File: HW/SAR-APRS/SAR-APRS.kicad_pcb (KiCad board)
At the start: 2 copper layers, 1 part

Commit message: update
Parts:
- removed A1: Arduino_Nano_v3.x, Modules:Arduino_Nano
- added U1: DRA818V, APRS_modules:DRA818, F.Cu at (190.2, 96.0)
- added U2: arduino_mini_clone, APRS_modules:arduino_mini_clone, F.Cu at (152.0, 96.0)

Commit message: update
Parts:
- added U3: ATMEGA328P-MMH, Housings_DFN_QFN:QFN-28-1EP_4x4mm_Pitch0.4mm, F.Cu at (162.1, 112.9)
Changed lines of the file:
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@@
     (tracks 0)
     (zones 0)
-    (modules 2)
-    (nets 57)
+    (modules 3)
+    (nets 85)
   )
   (page A4)
@@
   (net 55 "Net-(U1-Pad6)")
   (net 56 "Net-(U1-Pad7)")
+  (net 57 "Net-(U3-Pad1)")
+  (net 58 "Net-(U3-Pad2)")
+  (net 59 "Net-(U3-Pad3)")
+  (net 60 "Net-(U3-Pad4)")
+  (net 61 "Net-(U3-Pad5)")
+  (net 62 "Net-(U3-Pad6)")
+  (net 63 "Net-(U3-Pad7)")
+  (net 64 "Net-(U3-Pad8)")
+  (net 65 "Net-(U3-Pad9)")
+  (net 66 "Net-(U3-Pad10)")
+  (net 67 "Net-(U3-Pad11)")
+  (net 68 "Net-(U3-Pad12)")
+  (net 69 "Net-(U3-Pad13)")
+  (net 70 "Net-(U3-Pad14)")
+  (net 71 "Net-(U3-Pad15)")
+  (net 72 "Net-(U3-Pad16)")
+  (net 73 "Net-(U3-Pad17)")
+  (net 74 "Net-(U3-Pad18)")
+  (net 75 "Net-(U3-Pad19)")
+  (net 76 "Net-(U3-Pad20)")
+  (net 77 "Net-(U3-Pad21)")
+  (net 78 "Net-(U3-Pad22)")
+  (net 79 "Net-(U3-Pad23)")
+  (net 80 "Net-(U3-Pad24)")
+  (net 81 "Net-(U3-Pad25)")
+  (net 82 "Net-(U3-Pad26)")
+  (net 83 "Net-(U3-Pad27)")
+  (net 84 "Net-(U3-Pad28)")
   (net_class Default "This is the default net class."
     (clearance 0.2)
@@
     (add_net "Net-(U2-Pad8)")
     (add_net "Net-(U2-Pad9)")
+    (add_net "Net-(U3-Pad1)")
+    (add_net "Net-(U3-Pad10)")
+    (add_net "Net-(U3-Pad11)")
+    (add_net "Net-(U3-Pad12)")
+    (add_net "Net-(U3-Pad13)")
+    (add_net "Net-(U3-Pad14)")
+    (add_net "Net-(U3-Pad15)")
+    (add_net "Net-(U3-Pad16)")
+    (add_net "Net-(U3-Pad17)")
+    (add_net "Net-(U3-Pad18)")
+    (add_net "Net-(U3-Pad19)")
+    (add_net "Net-(U3-Pad2)")
+    (add_net "Net-(U3-Pad20)")
+    (add_net "Net-(U3-Pad21)")
+    (add_net "Net-(U3-Pad22)")
+    (add_net "Net-(U3-Pad23)")
+    (add_net "Net-(U3-Pad24)")
+    (add_net "Net-(U3-Pad25)")
+    (add_net "Net-(U3-Pad26)")
+    (add_net "Net-(U3-Pad27)")
+    (add_net "Net-(U3-Pad28)")
+    (add_net "Net-(U3-Pad3)")
+    (add_net "Net-(U3-Pad4)")
+    (add_net "Net-(U3-Pad5)")
+    (add_net "Net-(U3-Pad6)")
+    (add_net "Net-(U3-Pad7)")
+    (add_net "Net-(U3-Pad8)")
+    (add_net "Net-(U3-Pad9)")
+  )
+  (module Housings_DFN_QFN:QFN-28-1EP_4x4mm_Pitch0.4mm (layer F.Cu)
+    (at 162.1 112.9)
+    (descr "28-Lead Plastic Quad Flat, No Lead Package (MK) - 4x4x0.9 mm Body [QFN]; (see Microchip Packaging Specification 00000049BS.pdf)")
+    (tags "QFN 0.4")
+    (attr smd)
+    (fp_text reference U3 (at 0 -3.35) (layer F.SilkS)
+      (effects (font (size 1 1) (thickness 0.15)))
+    )
+    (fp_text value ATMEGA328P-MMH (at 0 3.35) (layer F.Fab)
+      (effects (font (size 1 1) (thickness 0.15)))
+    )
+    (fp_line (start -1 -2) (end 2 -2) (layer F.Fab) (width 0.15))
+    (fp_line (start 2 -2) (end 2 2) (layer F.Fab) (width 0.15))
+    (fp_line (start 2 2) (end -2 2) (layer F.Fab) (width 0.15))
+    (fp_line (start -2 2) (end -2 -1) (layer F.Fab) (width 0.15))
+    (fp_line (start -2 -1) (end -1 -2) (layer F.Fab) (width 0.15))
+    (fp_line (start -2.6 -2.6) (end -2.6 2.6) (layer F.CrtYd) (width 0.05))
+    (fp_line (start 2.6 -2.6) (end 2.6 2.6) (layer F.CrtYd) (width 0.05))
+    (fp_line (start -2.6 -2.6) (end 2.6 -2.6) (layer F.CrtYd) (width 0.05))
+    (fp_line (start -2.6 2.6) (end 2.6 2.6) (layer F.CrtYd) (width 0.05))
+    (fp_line (start 2.15 -2.15) (end 2.15 -1.525) (layer F.SilkS) (width 0.15))
+    (fp_line (start -2.15 2.15) (end -2.15 1.525) (layer F.SilkS) (width 0.15))
+    (fp_line (start 2.15 2.15) (end 2.15 1.525) (layer F.SilkS) (width 0.15))
+    (fp_line (start -2.15 -2.15) (end -1.525 -2.15) (layer F.SilkS) (width 0.15))
+    (fp_line (start -2.15 2.15) (end -1.525 2.15) (layer F.SilkS) (width 0.15))
+    (fp_line (start 2.15 2.15) (end 1.525 2.15) (layer F.SilkS) (width 0.15))
+    (fp_line (start 2.15 -2.15) (end 1.525 -2.15) (layer F.SilkS) (width 0.15))
+    (pad 1 smd rect (at -1.95 -1.2) (size 0.8 0.2) (layers F.Cu F.Paste F.Mask)
+      (net 57 "Net-(U3-Pad1)"))
+    (pad 2 smd rect (at -1.95 -0.8) (size 0.8 0.2) (layers F.Cu F.Paste F.Mask)
+      (net 58 "Net-(U3-Pad2)"))
+    (pad 3 smd rect (at -1.95 -0.4) (size 0.8 0.2) (layers F.Cu F.Paste F.Mask)
+      (net 59 "Net-(U3-Pad3)"))
+    (pad 4 smd rect (at -1.95 0) (size 0.8 0.2) (layers F.Cu F.Paste F.Mask)
+      (net 60 "Net-(U3-Pad4)"))
+    (pad 5 smd rect (at -1.95 0.4) (size 0.8 0.2) (layers F.Cu F.Paste F.Mask)
+      (net 61 "Net-(U3-Pad5)"))
+    (pad 6 smd rect (at -1.95 0.8) (size 0.8 0.2) (layers F.Cu F.Paste F.Mask)
+      (net 62 "Net-(U3-Pad6)"))
+    (pad 7 smd rect (at -1.95 1.2) (size 0.8 0.2) (layers F.Cu F.Paste F.Mask)
+      (net 63 "Net-(U3-Pad7)"))
+    (pad 8 smd rect (at -1.2 1.95 90) (size 0.8 0.2) (layers F.Cu F.Paste F.Mask)
+      (net 64 "Net-(U3-Pad8)"))
+    (pad 9 smd rect (at -0.8 1.95 90) (size 0.8 0.2) (layers F.Cu F.Paste F.Mask)
+      (net 65 "Net-(U3-Pad9)"))
+    (pad 10 smd rect (at -0.4 1.95 90) (size 0.8 0.2) (layers F.Cu F.Paste F.Mask)
+      (net 66 "Net-(U3-Pad10)"))
+    (pad 11 smd rect (at 0 1.95 90) (size 0.8 0.2) (layers F.Cu F.Paste F.Mask)
+      (net 67 "Net-(U3-Pad11)"))
+    (pad 12 smd rect (at 0.4 1.95 90) (size 0.8 0.2) (layers F.Cu F.Paste F.Mask)
+      (net 68 "Net-(U3-Pad12)"))
+    (pad 13 smd rect (at 0.8 1.95 90) (size 0.8 0.2) (layers F.Cu F.Paste F.Mask)
+      (net 69 "Net-(U3-Pad13)"))
+    (pad 14 smd rect (at 1.2 1.95 90) (size 0.8 0.2) (layers F.Cu F.Paste F.Mask)
+      (net 70 "Net-(U3-Pad14)"))
+    (pad 15 smd rect (at 1.95 1.2) (size 0.8 0.2) (layers F.Cu F.Paste F.Mask)
+      (net 71 "Net-(U3-Pad15)"))
+    (pad 16 smd rect (at 1.95 0.8) (size 0.8 0.2) (layers F.Cu F.Paste F.Mask)
+      (net 72 "Net-(U3-Pad16)"))
+    (pad 17 smd rect (at 1.95 0.4) (size 0.8 0.2) (layers F.Cu F.Paste F.Mask)
+      (net 73 "Net-(U3-Pad17)"))
+    (pad 18 smd rect (at 1.95 0) (size 0.8 0.2) (layers F.Cu F.Paste F.Mask)
+      (net 74 "Net-(U3-Pad18)"))
+    (pad 19 smd rect (at 1.95 -0.4) (size 0.8 0.2) (layers F.Cu F.Paste F.Mask)
+      (net 75 "Net-(U3-Pad19)"))
+    (pad 20 smd rect (at 1.95 -0.8) (size 0.8 0.2) (layers F.Cu F.Paste F.Mask)
+      (net 76 "Net-(U3-Pad20)"))
+    (pad 21 smd rect (at 1.95 -1.2) (size 0.8 0.2) (layers F.Cu F.Paste F.Mask)
+      (net 77 "Net-(U3-Pad21)"))
+    (pad 22 smd rect (at 1.2 -1.95 90) (size 0.8 0.2) (layers F.Cu F.Paste F.Mask)
+      (net 78 "Net-(U3-Pad22)"))
+    (pad 23 smd rect (at 0.8 -1.95 90) (size 0.8 0.2) (layers F.Cu F.Paste F.Mask)
+      (net 79 "Net-(U3-Pad23)"))
+    (pad 24 smd rect (at 0.4 -1.95 90) (size 0.8 0.2) (layers F.Cu F.Paste F.Mask)
+      (net 80 "Net-(U3-Pad24)"))
+    (pad 25 smd rect (at 0 -1.95 90) (size 0.8 0.2) (layers F.Cu F.Paste F.Mask)
+      (net 81 "Net-(U3-Pad25)"))
+    (pad 26 smd rect (at -0.4 -1.95 90) (size 0.8 0.2) (layers F.Cu F.Paste F.Mask)
+      (net 82 "Net-(U3-Pad26)"))
+    (pad 27 smd rect (at -0.8 -1.95 90) (size 0.8 0.2) (layers F.Cu F.Paste F.Mask)
+      (net 83 "Net-(U3-Pad27)"))
+    (pad 28 smd rect (at -1.2 -1.95 90) (size 0.8 0.2) (layers F.Cu F.Paste F.Mask)
+      (net 84 "Net-(U3-Pad28)"))
+    (pad 29 smd rect (at 0.6 0.6) (size 1.2 1.2) (layers F.Cu F.Paste F.Mask)
+      (solder_paste_margin_ratio -0.2))
+    (pad 29 smd rect (at 0.6 -0.6) (size 1.2 1.2) (layers F.Cu F.Paste F.Mask)
+      (solder_paste_margin_ratio -0.2))
+    (pad 29 smd rect (at -0.6 0.6) (size 1.2 1.2) (layers F.Cu F.Paste F.Mask)
+      (solder_paste_margin_ratio -0.2))
+    (pad 29 smd rect (at -0.6 -0.6) (size 1.2 1.2) (layers F.Cu F.Paste F.Mask)
+      (solder_paste_margin_ratio -0.2))
+    (model ${KISYS3DMOD}/Housings_DFN_QFN.3dshapes/QFN-28-1EP_4x4mm_Pitch0.4mm.wrl
+      (at (xyz 0 0 0))
+      (scale (xyz 1 1 1))
+      (rotate (xyz 0 0 0))
+    )
   )
   (module APRS_modules:DRA818 (layer F.Cu)

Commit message: update
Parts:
- removed U3: ATMEGA328P-MMH, Housings_DFN_QFN:QFN-28-1EP_4x4mm_Pitch0.4mm
- added J1: uFl, w_conn_rf:coaxial_u.fl-r-smt-1, F.Cu at (147.0, 78.0)
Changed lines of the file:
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@@
-(kicad_pcb (version 20171130) (host pcbnew "(6.0.0-rc1-dev-347-gd8782b751)")
+(kicad_pcb (version 20171130) (host pcbnew "(6.0.0-rc1-dev-909-gb389236a7)")
   (general
     (thickness 1.6)
@@
     (zones 0)
     (modules 3)
-    (nets 85)
+    (nets 59)
   )
   (page A4)
@@
     (pad_drill 0.762)
     (pad_to_mask_clearance 0.2)
+    (solder_mask_min_width 0.25)
     (aux_axis_origin 0 0)
     (visible_elements 7FFFFFFF)
@@
   (net 55 "Net-(U1-Pad6)")
   (net 56 "Net-(U1-Pad7)")
-  (net 57 "Net-(U3-Pad1)")
-  (net 58 "Net-(U3-Pad2)")
-  (net 59 "Net-(U3-Pad3)")
-  (net 60 "Net-(U3-Pad4)")
-  (net 61 "Net-(U3-Pad5)")
-  (net 62 "Net-(U3-Pad6)")
-  (net 63 "Net-(U3-Pad7)")
-  (net 64 "Net-(U3-Pad8)")
-  (net 65 "Net-(U3-Pad9)")
-  (net 66 "Net-(U3-Pad10)")
-  (net 67 "Net-(U3-Pad11)")
-  (net 68 "Net-(U3-Pad12)")
-  (net 69 "Net-(U3-Pad13)")
-  (net 70 "Net-(U3-Pad14)")
-  (net 71 "Net-(U3-Pad15)")
-  (net 72 "Net-(U3-Pad16)")
-  (net 73 "Net-(U3-Pad17)")
-  (net 74 "Net-(U3-Pad18)")
-  (net 75 "Net-(U3-Pad19)")
-  (net 76 "Net-(U3-Pad20)")
-  (net 77 "Net-(U3-Pad21)")
-  (net 78 "Net-(U3-Pad22)")
-  (net 79 "Net-(U3-Pad23)")
-  (net 80 "Net-(U3-Pad24)")
-  (net 81 "Net-(U3-Pad25)")
-  (net 82 "Net-(U3-Pad26)")
-  (net 83 "Net-(U3-Pad27)")
-  (net 84 "Net-(U3-Pad28)")
+  (net 57 "Net-(J1-Pad1)")
+  (net 58 GND)
   (net_class Default "This is the default net class."
     (clearance 0.2)
@@
     (uvia_dia 0.3)
     (uvia_drill 0.1)
+    (add_net GND)
+    (add_net "Net-(J1-Pad1)")
     (add_net "Net-(U1-Pad1)")
     (add_net "Net-(U1-Pad10)")
@@
     (add_net "Net-(U2-Pad8)")
     (add_net "Net-(U2-Pad9)")
-    (add_net "Net-(U3-Pad1)")
-    (add_net "Net-(U3-Pad10)")
-    (add_net "Net-(U3-Pad11)")
-    (add_net "Net-(U3-Pad12)")
-    (add_net "Net-(U3-Pad13)")
-    (add_net "Net-(U3-Pad14)")
-    (add_net "Net-(U3-Pad15)")
-    (add_net "Net-(U3-Pad16)")
-    (add_net "Net-(U3-Pad17)")
-    (add_net "Net-(U3-Pad18)")
-    (add_net "Net-(U3-Pad19)")
-    (add_net "Net-(U3-Pad2)")
-    (add_net "Net-(U3-Pad20)")
-    (add_net "Net-(U3-Pad21)")
-    (add_net "Net-(U3-Pad22)")
-    (add_net "Net-(U3-Pad23)")
-    (add_net "Net-(U3-Pad24)")
-    (add_net "Net-(U3-Pad25)")
-    (add_net "Net-(U3-Pad26)")
-    (add_net "Net-(U3-Pad27)")
-    (add_net "Net-(U3-Pad28)")
-    (add_net "Net-(U3-Pad3)")
-    (add_net "Net-(U3-Pad4)")
-    (add_net "Net-(U3-Pad5)")
-    (add_net "Net-(U3-Pad6)")
-    (add_net "Net-(U3-Pad7)")
-    (add_net "Net-(U3-Pad8)")
-    (add_net "Net-(U3-Pad9)")
-  )
-  (module Housings_DFN_QFN:QFN-28-1EP_4x4mm_Pitch0.4mm (layer F.Cu)
-    (at 162.1 112.9)
-    (descr "28-Lead Plastic Quad Flat, No Lead Package (MK) - 4x4x0.9 mm Body [QFN]; (see Microchip Packaging Specification 00000049BS.pdf)")
-    (tags "QFN 0.4")
-    (attr smd)
-    (fp_text reference U3 (at 0 -3.35) (layer F.SilkS)
-      (effects (font (size 1 1) (thickness 0.15)))
+  )
+  (module w_conn_rf:coaxial_u.fl-r-smt-1 (layer F.Cu)
+    (at 147 78)
+    (descr "Ultra small surface mount coaxial connector, Hirose U.FL-R-SMT-1")
+    (fp_text reference J1 (at 0 -2.1) (layer F.SilkS)
+      (effects (font (size 0.5 0.5) (thickness 0.1)))
     )
-    (fp_text value ATMEGA328P-MMH (at 0 3.35) (layer F.Fab)
-      (effects (font (size 1 1) (thickness 0.15)))
+    (fp_text value uFl (at 0 2.7) (layer F.SilkS)
+      (effects (font (size 0.5 0.5) (thickness 0.1)))
     )
-    (fp_line (start -1 -2) (end 2 -2) (layer F.Fab) (width 0.15))
-    (fp_line (start 2 -2) (end 2 2) (layer F.Fab) (width 0.15))
-    (fp_line (start 2 2) (end -2 2) (layer F.Fab) (width 0.15))
-    (fp_line (start -2 2) (end -2 -1) (layer F.Fab) (width 0.15))
-    (fp_line (start -2 -1) (end -1 -2) (layer F.Fab) (width 0.15))
-    (fp_line (start -2.6 -2.6) (end -2.6 2.6) (layer F.CrtYd) (width 0.05))
-    (fp_line (start 2.6 -2.6) (end 2.6 2.6) (layer F.CrtYd) (width 0.05))
-    (fp_line (start -2.6 -2.6) (end 2.6 -2.6) (layer F.CrtYd) (width 0.05))
-    (fp_line (start -2.6 2.6) (end 2.6 2.6) (layer F.CrtYd) (width 0.05))
-    (fp_line (start 2.15 -2.15) (end 2.15 -1.525) (layer F.SilkS) (width 0.15))
-    (fp_line (start -2.15 2.15) (end -2.15 1.525) (layer F.SilkS) (width 0.15))
-    (fp_line (start 2.15 2.15) (end 2.15 1.525) (layer F.SilkS) (width 0.15))
-    (fp_line (start -2.15 -2.15) (end -1.525 -2.15) (layer F.SilkS) (width 0.15))
-    (fp_line (start -2.15 2.15) (end -1.525 2.15) (layer F.SilkS) (width 0.15))
-    (fp_line (start 2.15 2.15) (end 1.525 2.15) (layer F.SilkS) (width 0.15))
-    (fp_line (start 2.15 -2.15) (end 1.525 -2.15) (layer F.SilkS) (width 0.15))
-    (pad 1 smd rect (at -1.95 -1.2) (size 0.8 0.2) (layers F.Cu F.Paste F.Mask)
-      (net 57 "Net-(U3-Pad1)"))
-    (pad 2 smd rect (at -1.95 -0.8) (size 0.8 0.2) (layers F.Cu F.Paste F.Mask)
-      (net 58 "Net-(U3-Pad2)"))
-    (pad 3 smd rect (at -1.95 -0.4) (size 0.8 0.2) (layers F.Cu F.Paste F.Mask)
-      (net 59 "Net-(U3-Pad3)"))
-    (pad 4 smd rect (at -1.95 0) (size 0.8 0.2) (layers F.Cu F.Paste F.Mask)
-      (net 60 "Net-(U3-Pad4)"))
-    (pad 5 smd rect (at -1.95 0.4) (size 0.8 0.2) (layers F.Cu F.Paste F.Mask)
-      (net 61 "Net-(U3-Pad5)"))
-    (pad 6 smd rect (at -1.95 0.8) (size 0.8 0.2) (layers F.Cu F.Paste F.Mask)
-      (net 62 "Net-(U3-Pad6)"))
-    (pad 7 smd rect (at -1.95 1.2) (size 0.8 0.2) (layers F.Cu F.Paste F.Mask)
-      (net 63 "Net-(U3-Pad7)"))
-    (pad 8 smd rect (at -1.2 1.95 90) (size 0.8 0.2) (layers F.Cu F.Paste F.Mask)
-      (net 64 "Net-(U3-Pad8)"))
-    (pad 9 smd rect (at -0.8 1.95 90) (size 0.8 0.2) (layers F.Cu F.Paste F.Mask)
-      (net 65 "Net-(U3-Pad9)"))
-    (pad 10 smd rect (at -0.4 1.95 90) (size 0.8 0.2) (layers F.Cu F.Paste F.Mask)
-      (net 66 "Net-(U3-Pad10)"))
-    (pad 11 smd rect (at 0 1.95 90) (size 0.8 0.2) (layers F.Cu F.Paste F.Mask)
-      (net 67 "Net-(U3-Pad11)"))
-    (pad 12 smd rect (at 0.4 1.95 90) (size 0.8 0.2) (layers F.Cu F.Paste F.Mask)
-      (net 68 "Net-(U3-Pad12)"))
-    (pad 13 smd rect (at 0.8 1.95 90) (size 0.8 0.2) (layers F.Cu F.Paste F.Mask)
-      (net 69 "Net-(U3-Pad13)"))
-    (pad 14 smd rect (at 1.2 1.95 90) (size 0.8 0.2) (layers F.Cu F.Paste F.Mask)
-      (net 70 "Net-(U3-Pad14)"))
-    (pad 15 smd rect (at 1.95 1.2) (size 0.8 0.2) (layers F.Cu F.Paste F.Mask)
-      (net 71 "Net-(U3-Pad15)"))
-    (pad 16 smd rect (at 1.95 0.8) (size 0.8 0.2) (layers F.Cu F.Paste F.Mask)
-      (net 72 "Net-(U3-Pad16)"))
-    (pad 17 smd rect (at 1.95 0.4) (size 0.8 0.2) (layers F.Cu F.Paste F.Mask)
-      (net 73 "Net-(U3-Pad17)"))
-    (pad 18 smd rect (at 1.95 0) (size 0.8 0.2) (layers F.Cu F.Paste F.Mask)
-      (net 74 "Net-(U3-Pad18)"))
-    (pad 19 smd rect (at 1.95 -0.4) (size 0.8 0.2) (layers F.Cu F.Paste F.Mask)
-      (net 75 "Net-(U3-Pad19)"))
-    (pad 20 smd rect (at 1.95 -0.8) (size 0.8 0.2) (layers F.Cu F.Paste F.Mask)
-      (net 76 "Net-(U3-Pad20)"))
-    (pad 21 smd rect (at 1.95 -1.2) (size 0.8 0.2) (layers F.Cu F.Paste F.Mask)
-      (net 77 "Net-(U3-Pad21)"))
-    (pad 22 smd rect (at 1.2 -1.95 90) (size 0.8 0.2) (layers F.Cu F.Paste F.Mask)
-      (net 78 "Net-(U3-Pad22)"))
-    (pad 23 smd rect (at 0.8 -1.95 90) (size 0.8 0.2) (layers F.Cu F.Paste F.Mask)
-      (net 79 "Net-(U3-Pad23)"))
-    (pad 24 smd rect (at 0.4 -1.95 90) (size 0.8 0.2) (layers F.Cu F.Paste F.Mask)
-      (net 80 "Net-(U3-Pad24)"))
-    (pad 25 smd rect (at 0 -1.95 90) (size 0.8 0.2) (layers F.Cu F.Paste F.Mask)
-      (net 81 "Net-(U3-Pad25)"))
-    (pad 26 smd rect (at -0.4 -1.95 90) (size 0.8 0.2) (layers F.Cu F.Paste F.Mask)
-      (net 82 "Net-(U3-Pad26)"))
-    (pad 27 smd rect (at -0.8 -1.95 90) (size 0.8 0.2) (layers F.Cu F.Paste F.Mask)
-      (net 83 "Net-(U3-Pad27)"))
-    (pad 28 smd rect (at -1.2 -1.95 90) (size 0.8 0.2) (layers F.Cu F.Paste F.Mask)
-      (net 84 "Net-(U3-Pad28)"))
-    (pad 29 smd rect (at 0.6 0.6) (size 1.2 1.2) (layers F.Cu F.Paste F.Mask)
-      (solder_paste_margin_ratio -0.2))
-    (pad 29 smd rect (at 0.6 -0.6) (size 1.2 1.2) (layers F.Cu F.Paste F.Mask)
-      (solder_paste_margin_ratio -0.2))
-    (pad 29 smd rect (at -0.6 0.6) (size 1.2 1.2) (layers F.Cu F.Paste F.Mask)
-      (solder_paste_margin_ratio -0.2))
-    (pad 29 smd rect (at -0.6 -0.6) (size 1.2 1.2) (layers F.Cu F.Paste F.Mask)
-      (solder_paste_margin_ratio -0.2))
-    (model ${KISYS3DMOD}/Housings_DFN_QFN.3dshapes/QFN-28-1EP_4x4mm_Pitch0.4mm.wrl
+    (fp_arc (start -1 -1) (end -1.3 -1) (angle 90) (layer F.SilkS) (width 0.15))
+    (fp_arc (start 1 -1) (end 1 -1.3) (angle 90) (layer F.SilkS) (width 0.15))
+    (fp_arc (start 1 1) (end 1.3 1) (angle 90) (layer F.SilkS) (width 0.15))
+    (fp_arc (start -1 1) (end -1 1.3) (angle 90) (layer F.SilkS) (width 0.15))
+    (fp_line (start -1 -1.3) (end 1 -1.3) (layer F.SilkS) (width 0.15))
+    (fp_line (start 1.3 -1) (end 1.3 1) (layer F.SilkS) (width 0.15))
+    (fp_line (start 1 1.3) (end -1 1.3) (layer F.SilkS) (width 0.15))
+    (fp_line (start -1.3 1) (end -1.3 -1) (layer F.SilkS) (width 0.15))
+    (fp_circle (center 0 0) (end -1 0) (layer F.SilkS) (width 0.15))
+    (fp_circle (center 0 0) (end -0.1 0) (layer F.SilkS) (width 0.15))
+    (pad 1 smd rect (at 0 1.525) (size 1 1.05) (layers F.Cu F.Paste F.Mask)
+      (net 57 "Net-(J1-Pad1)") (solder_mask_margin 0.07) (solder_paste_margin -0.05))
+    (pad 2 smd rect (at 1.475 0) (size 1.05 2.2) (layers F.Cu F.Paste F.Mask)
+      (net 58 GND) (solder_mask_margin 0.07) (solder_paste_margin -0.05))
+    (pad 2 smd rect (at -1.475 0) (size 1.05 2.2) (layers F.Cu F.Paste F.Mask)
+      (net 58 GND) (solder_mask_margin 0.07) (solder_paste_margin -0.05))
+    (model walter/conn_rf/coaxial_u.fl-r-smt-1.wrl
       (at (xyz 0 0 0))
       (scale (xyz 1 1 1))

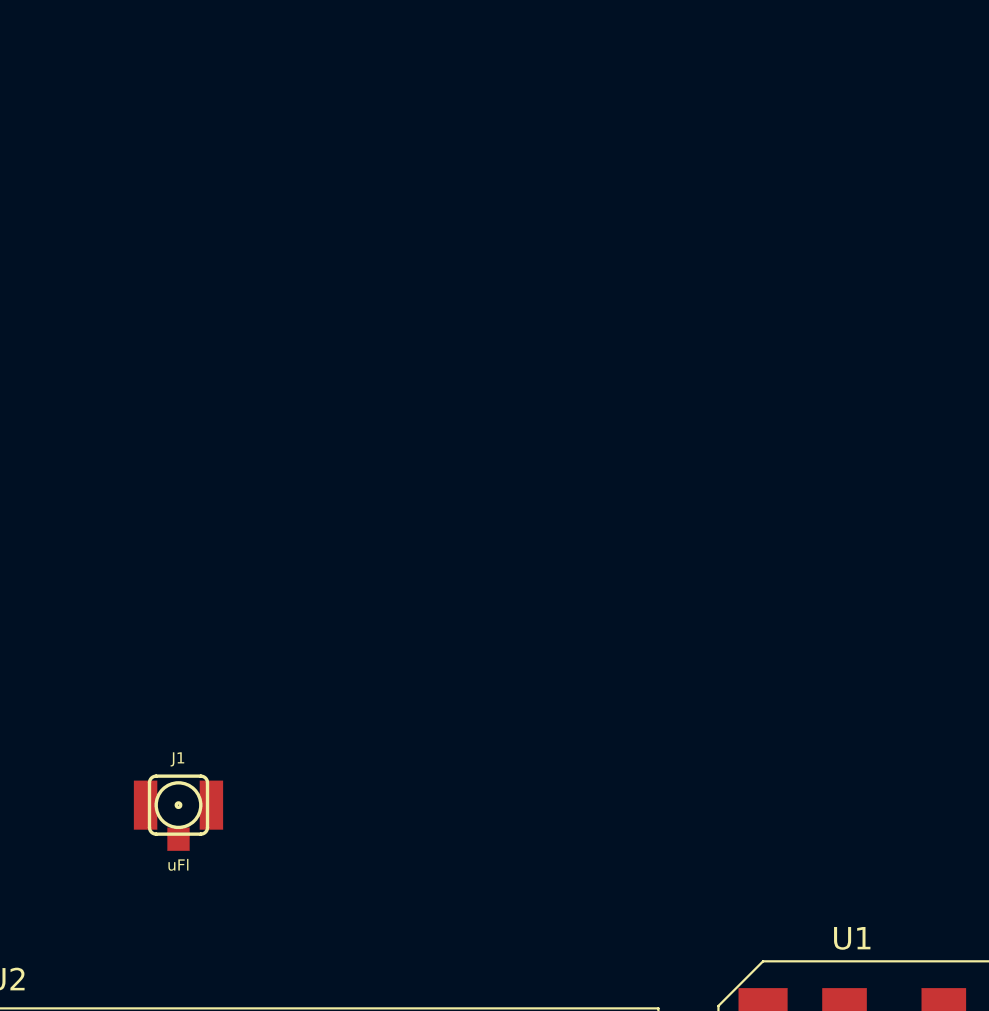
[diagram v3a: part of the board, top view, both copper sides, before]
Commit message: schematic update
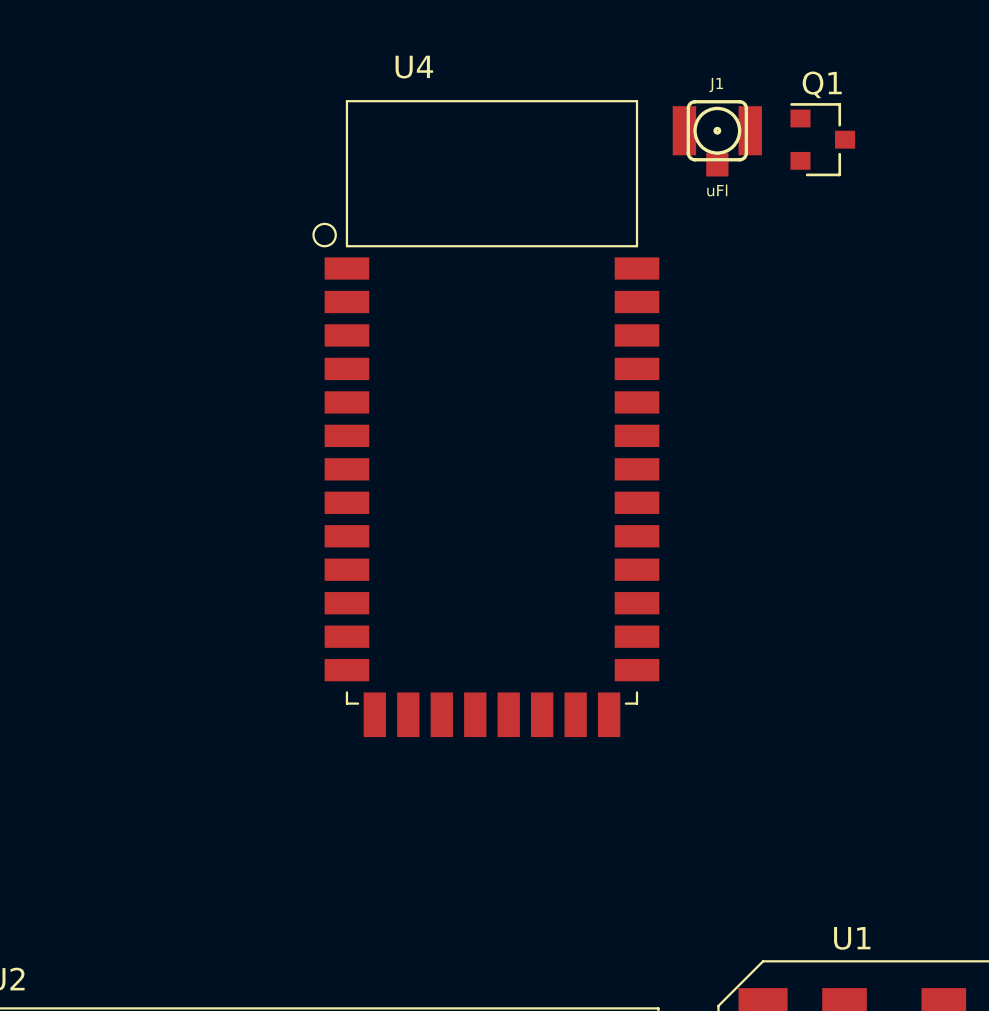
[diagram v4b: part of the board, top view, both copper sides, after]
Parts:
- added Q1: 2N7002, TO_SOT_Packages_SMD:SOT-23, F.Cu at (175.9, 48.2)
- added U4: HC-05, maxrez:HC-05 BT, F.Cu at (161.1, 54.0)
- moved J1 38.7 mm to (171.2, 47.8)
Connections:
- U1 pad 10: Net-(U1-Pad10) -> GND
- U1 pad 8: Net-(U1-Pad8) -> +3V8
- U1 pad 9: Net-(U1-Pad9) -> GND
- U1 pad P2: Net-(U1-PadP2) -> GND
- U1 pad P3: Net-(U1-PadP3) -> GND
- U2 pad 1: Net-(U2-Pad1) -> GND
- U2 pad 12: Net-(U2-Pad12) -> +3V3
- U2 pad 14: Net-(U2-Pad14) -> GND
- U2 pad 15: Net-(U2-Pad15) -> +3V8
- U2 pad 16: Net-(U2-Pad16) -> GND
- U2 pad 17: Net-(U2-Pad17) -> GND
- U2 pad 25: Net-(U2-Pad25) -> GND
- U2 pad 6: Net-(U2-Pad6) -> Net-(U1-Pad16)
- U2 pad 7: Net-(U2-Pad7) -> Net-(U1-Pad17)

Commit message: schematic update
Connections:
- net +3V8 renamed Bat+
- net GND renamed Bat-
- U2 pad 30: Net-(U2-Pad30) -> Net-(R10-Pad2)
- U4 pad 34: Net-(U4-Pad34) -> Net-(R10-Pad2)
